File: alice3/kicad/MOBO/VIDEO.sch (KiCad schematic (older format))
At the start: 15 parts, among them P1 CONN_01X05, SW1 RESET, U1 LM2937-3.3, U2 VGA_daughter_board, U3 Propeller_P8X32A-D40, U4 24LC256, U5 Propeller_Plug, Y1 5 MHz

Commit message: Remove on/off switch.
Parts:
- C1: footprint Capacitors_ThroughHole:C_Radial_D13_L21_P5 -> Capacitors_ThroughHole:C_Radial_D8_L11.5_P3.5
- P1: footprint (none) -> Pin_Headers:Pin_Header_Angled_1x05
- Y1: footprint Crystals:Crystal_HC48-U_Vertical -> Crystals:Crystal_HC50-U_Vertical
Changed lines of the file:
@@
 $EndComp
 $Comp
-L GND #PWR10
+L GND #PWR01
 U 1 1 566E4A0D
 P 6100 4700
-F 0 "#PWR10" H 6100 4450 50  0001 C CNN
+F 0 "#PWR01" H 6100 4450 50  0001 C CNN
 F 1 "GND" H 6100 4550 50  0000 C CNN
 F 2 "" H 6100 4700 50  0000 C CNN
@@
 $EndComp
 $Comp
-L +3.3V #PWR9
+L +3.3V #PWR02
 U 1 1 566E4A37
 P 6100 2100
-F 0 "#PWR9" H 6100 1950 50  0001 C CNN
+F 0 "#PWR02" H 6100 1950 50  0001 C CNN
 F 1 "+3.3V" H 6100 2240 50  0000 C CNN
 F 2 "" H 6100 2100 50  0000 C CNN
@@
 F 0 "Y1" H 7750 4600 50  0000 C CNN
 F 1 "5 MHz" H 7750 4300 50  0000 C CNN
-F 2 "Crystals:Crystal_HC48-U_Vertical" H 7750 4450 50  0001 C CNN
+F 2 "Crystals:Crystal_HC50-U_Vertical" H 7750 4450 50  0001 C CNN
 F 3 "" H 7750 4450 50  0000 C CNN
 	1    7750 4450
@@
 $EndComp
 $Comp
-L GND #PWR14
+L GND #PWR03
 U 1 1 566E4C07
 P 8650 2400
-F 0 "#PWR14" H 8650 2150 50  0001 C CNN
+F 0 "#PWR03" H 8650 2150 50  0001 C CNN
 F 1 "GND" H 8650 2250 50  0000 C CNN
 F 2 "" H 8650 2400 50  0000 C CNN
@@
 $EndComp
 $Comp
-L GND #PWR13
+L GND #PWR04
 U 1 1 5681F164
 P 8350 4400
-F 0 "#PWR13" H 8350 4150 50  0001 C CNN
+F 0 "#PWR04" H 8350 4150 50  0001 C CNN
 F 1 "GND" H 8350 4250 50  0000 C CNN
 F 2 "" H 8350 4400 50  0000 C CNN
@@
 $EndComp
 $Comp
-L +3.3V #PWR15
+L +3.3V #PWR05
 U 1 1 5681F2C2
 P 9450 3850
-F 0 "#PWR15" H 9450 3700 50  0001 C CNN
+F 0 "#PWR05" H 9450 3700 50  0001 C CNN
 F 1 "+3.3V" H 9450 3990 50  0000 C CNN
 F 2 "" H 9450 3850 50  0000 C CNN
@@
 $EndComp
 $Comp
-L GND #PWR16
+L GND #PWR06
 U 1 1 5681F2E8
 P 9700 4150
-F 0 "#PWR16" H 9700 3900 50  0001 C CNN
+F 0 "#PWR06" H 9700 3900 50  0001 C CNN
 F 1 "GND" H 9700 4000 50  0000 C CNN
 F 2 "" H 9700 4150 50  0000 C CNN
@@
 $EndComp
 $Comp
-L +3.3V #PWR12
+L +3.3V #PWR07
 U 1 1 5681F435
 P 8100 3600
-F 0 "#PWR12" H 8100 3450 50  0001 C CNN
+F 0 "#PWR07" H 8100 3450 50  0001 C CNN
 F 1 "+3.3V" H 8100 3740 50  0000 C CNN
 F 2 "" H 8100 3600 50  0000 C CNN
@@
 $EndComp
 $Comp
-L GND #PWR2
+L GND #PWR08
 U 1 1 5681F91B
 P 2950 2350
-F 0 "#PWR2" H 2950 2100 50  0001 C CNN
+F 0 "#PWR08" H 2950 2100 50  0001 C CNN
 F 1 "GND" H 2950 2200 50  0000 C CNN
 F 2 "" H 2950 2350 50  0000 C CNN
@@
 $EndComp
 $Comp
-L +5V #PWR1
+L +5V #PWR09
 U 1 1 5681FA03
 P 2350 1650
-F 0 "#PWR1" H 2350 1500 50  0001 C CNN
+F 0 "#PWR09" H 2350 1500 50  0001 C CNN
 F 1 "+5V" H 2350 1790 50  0000 C CNN
 F 2 "" H 2350 1650 50  0000 C CNN
@@
 $EndComp
 $Comp
-L +3.3V #PWR3
+L +3.3V #PWR010
 U 1 1 5681FA32
 P 3550 1650
-F 0 "#PWR3" H 3550 1500 50  0001 C CNN
+F 0 "#PWR010" H 3550 1500 50  0001 C CNN
 F 1 "+3.3V" H 3550 1790 50  0000 C CNN
 F 2 "" H 3550 1650 50  0000 C CNN
@@
 F 0 "C1" H 3575 2100 50  0000 L CNN
 F 1 "1000 µF" H 3575 1900 50  0000 L CNN
-F 2 "Capacitors_ThroughHole:C_Radial_D13_L21_P5" H 3550 2000 50  0001 C CNN
+F 2 "Capacitors_ThroughHole:C_Radial_D8_L11.5_P3.5" H 3550 2000 50  0001 C CNN
 F 3 "" H 3550 2000 50  0000 C CNN
 	1    3550 2000
@@
 $EndComp
 $Comp
-L GND #PWR4
+L GND #PWR011
 U 1 1 56821F3F
 P 5100 2700
-F 0 "#PWR4" H 5100 2450 50  0001 C CNN
+F 0 "#PWR011" H 5100 2450 50  0001 C CNN
 F 1 "GND" H 5100 2550 50  0000 C CNN
 F 2 "" H 5100 2700 50  0000 C CNN
@@
 $EndComp
 $Comp
-L GND #PWR11
+L GND #PWR012
 U 1 1 56826035
 P 7450 2400
-F 0 "#PWR11" H 7450 2150 50  0001 C CNN
+F 0 "#PWR012" H 7450 2150 50  0001 C CNN
 F 1 "GND" H 7450 2250 50  0000 C CNN
 F 2 "" H 7450 2400 50  0000 C CNN
@@
 	8300 2500 7850 2500
 $Comp
-L GND #PWR5
+L GND #PWR013
 U 1 1 568DCD28
 P 5600 4800
-F 0 "#PWR5" H 5600 4550 50  0001 C CNN
+F 0 "#PWR013" H 5600 4550 50  0001 C CNN
 F 1 "GND" H 5600 4650 50  0000 C CNN
 F 2 "" H 5600 4800 50  0000 C CNN
@@
 	5500 4800 5600 4800
 $Comp
-L +5V #PWR8
+L +5V #PWR014
 U 1 1 568DCDF3
 P 5900 4850
-F 0 "#PWR8" H 5900 4700 50  0001 C CNN
+F 0 "#PWR014" H 5900 4700 50  0001 C CNN
 F 1 "+5V" H 5900 4990 50  0000 C CNN
 F 2 "" H 5900 4850 50  0000 C CNN
@@
 $EndComp
 $Comp
-L GND #PWR7
+L GND #PWR015
 U 1 1 568DD571
 P 5800 2200
-F 0 "#PWR7" H 5800 1950 50  0001 C CNN
+F 0 "#PWR015" H 5800 1950 50  0001 C CNN
 F 1 "GND" H 5800 2050 50  0000 C CNN
 F 2 "" H 5800 2200 50  0000 C CNN
@@
 $EndComp
 $Comp
-L +3.3V #PWR6
+L +3.3V #PWR016
 U 1 1 568DD5A9
 P 5800 1700
-F 0 "#PWR6" H 5800 1550 50  0001 C CNN
+F 0 "#PWR016" H 5800 1550 50  0001 C CNN
 F 1 "+3.3V" H 5800 1840 50  0000 C CNN
 F 2 "" H 5800 1700 50  0000 C CNN
@@
 F 0 "P1" H 3200 3900 50  0000 C CNN
 F 1 "CONN_01X05" V 3300 3600 50  0000 C CNN
-F 2 "" H 3200 3600 50  0000 C CNN
+F 2 "Pin_Headers:Pin_Header_Angled_1x05" H 3200 3600 50  0001 C CNN
 F 3 "" H 3200 3600 50  0000 C CNN
 	1    3200 3600
@@
 $EndComp
 $Comp
-L GND #PWR?
+L GND #PWR017
 U 1 1 56A0506B
 P 3400 3900
-F 0 "#PWR?" H 3400 3650 50  0001 C CNN
+F 0 "#PWR017" H 3400 3650 50  0001 C CNN
 F 1 "GND" H 3400 3750 50  0000 C CNN
 F 2 "" H 3400 3900 50  0000 C CNN
@@
 $EndComp
 $Comp
-L +3.3V #PWR?
+L +3.3V #PWR018
 U 1 1 56A050A3
 P 3700 3900
-F 0 "#PWR?" H 3700 3750 50  0001 C CNN
+F 0 "#PWR018" H 3700 3750 50  0001 C CNN
 F 1 "+3.3V" H 3700 4040 50  0000 C CNN
 F 2 "" H 3700 3900 50  0000 C CNN

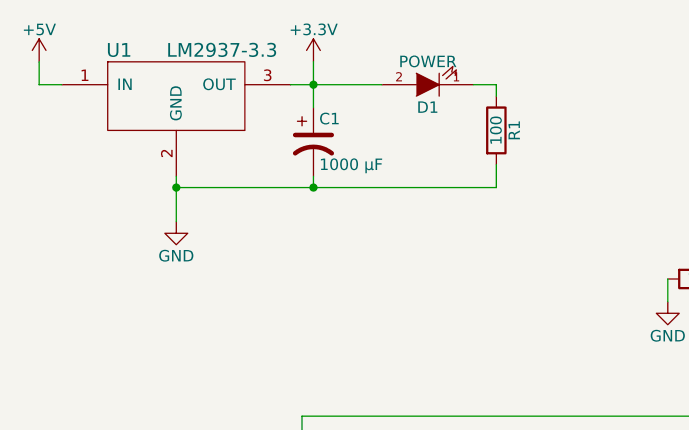
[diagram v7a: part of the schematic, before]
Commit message: Remove DFROBOT and LDO.
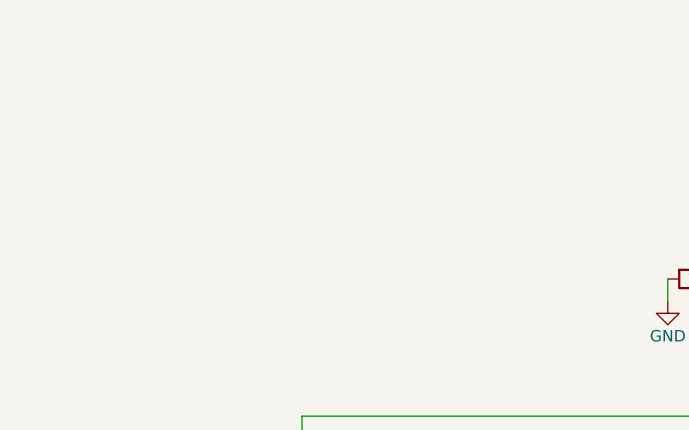
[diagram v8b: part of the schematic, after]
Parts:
- removed C1: 1000 µF, Capacitors_ThroughHole:C_Radial_D8_L11.5_P3.5, symbol CP1
- removed D1: POWER, LEDs:LED-5MM, symbol LED
- removed R1: 100, Resistors_ThroughHole:Resistor_Horizontal_RM10mm, symbol R
- removed U1: LM2937-3.3, Power_Integrations:TO-220, symbol LM2937-3.3
- U5: footprint Pin_Headers:Pin_Header_Straight_1x04 -> Pin_Headers:Pin_Header_Angled_1x04
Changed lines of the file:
@@
 $EndComp
 $Comp
-L GND #PWR12
+L GND #PWR01
 U 1 1 566E4A0D
 P 6100 4700
-F 0 "#PWR12" H 6100 4450 50  0001 C CNN
+F 0 "#PWR01" H 6100 4450 50  0001 C CNN
 F 1 "GND" H 6100 4550 50  0000 C CNN
 F 2 "" H 6100 4700 50  0000 C CNN
@@
 $EndComp
 $Comp
-L +3.3V #PWR11
+L +3.3V #PWR02
 U 1 1 566E4A37
 P 6100 2100
-F 0 "#PWR11" H 6100 1950 50  0001 C CNN
+F 0 "#PWR02" H 6100 1950 50  0001 C CNN
 F 1 "+3.3V" H 6100 2240 50  0000 C CNN
 F 2 "" H 6100 2100 50  0000 C CNN
@@
 $EndComp
 $Comp
-L GND #PWR16
+L GND #PWR03
 U 1 1 566E4C07
 P 8650 2400
-F 0 "#PWR16" H 8650 2150 50  0001 C CNN
+F 0 "#PWR03" H 8650 2150 50  0001 C CNN
 F 1 "GND" H 8650 2250 50  0000 C CNN
 F 2 "" H 8650 2400 50  0000 C CNN
@@
 $EndComp
 $Comp
-L GND #PWR15
+L GND #PWR04
 U 1 1 5681F164
 P 8350 4400
-F 0 "#PWR15" H 8350 4150 50  0001 C CNN
+F 0 "#PWR04" H 8350 4150 50  0001 C CNN
 F 1 "GND" H 8350 4250 50  0000 C CNN
 F 2 "" H 8350 4400 50  0000 C CNN
@@
 $EndComp
 $Comp
-L +3.3V #PWR17
+L +3.3V #PWR05
 U 1 1 5681F2C2
 P 9450 3850
-F 0 "#PWR17" H 9450 3700 50  0001 C CNN
+F 0 "#PWR05" H 9450 3700 50  0001 C CNN
 F 1 "+3.3V" H 9450 3990 50  0000 C CNN
 F 2 "" H 9450 3850 50  0000 C CNN
@@
 $EndComp
 $Comp
-L GND #PWR18
+L GND #PWR06
 U 1 1 5681F2E8
 P 9700 4150
-F 0 "#PWR18" H 9700 3900 50  0001 C CNN
+F 0 "#PWR06" H 9700 3900 50  0001 C CNN
 F 1 "GND" H 9700 4000 50  0000 C CNN
 F 2 "" H 9700 4150 50  0000 C CNN
@@
 $EndComp
 $Comp
-L +3.3V #PWR14
+L +3.3V #PWR07
 U 1 1 5681F435
 P 8100 3600
-F 0 "#PWR14" H 8100 3450 50  0001 C CNN
+F 0 "#PWR07" H 8100 3450 50  0001 C CNN
 F 1 "+3.3V" H 8100 3740 50  0000 C CNN
 F 2 "" H 8100 3600 50  0000 C CNN
@@
 F 0 "U5" H 9500 3150 60  0000 C CNN
 F 1 "Propeller_Plug" H 9650 2500 60  0000 C CNN
-F 2 "Pin_Headers:Pin_Header_Straight_1x04" H 9600 2850 60  0001 C CNN
+F 2 "Pin_Headers:Pin_Header_Angled_1x04" H 9600 2850 60  0001 C CNN
 F 3 "" H 9600 2850 60  0000 C CNN
 	1    9600 2850
-	1    0    0    -1
-$EndComp
-$Comp
-L LM2937-3.3 U1
-U 1 1 5681F8BE
-P 2950 1800
-F 0 "U1" H 2700 2000 60  0000 C CNN
-F 1 "LM2937-3.3" H 3150 2000 60  0000 C CNN
-F 2 "Power_Integrations:TO-220" H 2950 1800 60  0001 C CNN
-F 3 "" H 2950 1800 60  0000 C CNN
-	1    2950 1800
-	1    0    0    -1
-$EndComp
-$Comp
-L GND #PWR2
-U 1 1 5681F91B
-P 2950 2350
-F 0 "#PWR2" H 2950 2100 50  0001 C CNN
-F 1 "GND" H 2950 2200 50  0000 C CNN
-F 2 "" H 2950 2350 50  0000 C CNN
-F 3 "" H 2950 2350 50  0000 C CNN
-	1    2950 2350
-	1    0    0    -1
-$EndComp
-$Comp
-L +5V #PWR1
-U 1 1 5681FA03
-P 2350 1650
-F 0 "#PWR1" H 2350 1500 50  0001 C CNN
-F 1 "+5V" H 2350 1790 50  0000 C CNN
-F 2 "" H 2350 1650 50  0000 C CNN
-F 3 "" H 2350 1650 50  0000 C CNN
-	1    2350 1650
-	1    0    0    -1
-$EndComp
-$Comp
-L +3.3V #PWR4
-U 1 1 5681FA32
-P 3550 1650
-F 0 "#PWR4" H 3550 1500 50  0001 C CNN
-F 1 "+3.3V" H 3550 1790 50  0000 C CNN
-F 2 "" H 3550 1650 50  0000 C CNN
-F 3 "" H 3550 1650 50  0000 C CNN
-	1    3550 1650
-	1    0    0    -1
-$EndComp
-$Comp
-L CP1 C1
-U 1 1 5681FB9D
-P 3550 2000
-F 0 "C1" H 3575 2100 50  0000 L CNN
-F 1 "1000 µF" H 3575 1900 50  0000 L CNN
-F 2 "Capacitors_ThroughHole:C_Radial_D8_L11.5_P3.5" H 3550 2000 50  0001 C CNN
-F 3 "" H 3550 2000 50  0000 C CNN
-	1    3550 2000
-	1    0    0    -1
-$EndComp
-$Comp
-L LED D1
-U 1 1 5681FD4E
-P 4050 1750
-F 0 "D1" H 4050 1850 50  0000 C CNN
-F 1 "POWER" H 4050 1650 50  0000 C CNN
-F 2 "LEDs:LED-5MM" H 4050 1750 50  0001 C CNN
-F 3 "" H 4050 1750 50  0000 C CNN
-	1    4050 1750
-	-1   0    0    1
-$EndComp
-$Comp
-L R R1
-U 1 1 5681FD9C
-P 4350 1950
-F 0 "R1" V 4430 1950 50  0000 C CNN
-F 1 "100" V 4350 1950 50  0000 C CNN
-F 2 "Resistors_ThroughHole:Resistor_Horizontal_RM10mm" V 4280 1950 50  0001 C CNN
-F 3 "" H 4350 1950 50  0000 C CNN
-	1    4350 1950
 	1    0    0    -1
 $EndComp
@@
 $EndComp
 $Comp
-L GND #PWR6
+L GND #PWR08
 U 1 1 56821F3F
 P 5100 2700
-F 0 "#PWR6" H 5100 2450 50  0001 C CNN
+F 0 "#PWR08" H 5100 2450 50  0001 C CNN
 F 1 "GND" H 5100 2550 50  0000 C CNN
 F 2 "" H 5100 2700 50  0000 C CNN
@@
 $EndComp
 $Comp
-L GND #PWR13
+L GND #PWR09
 U 1 1 56826035
 P 7450 2400
-F 0 "#PWR13" H 7450 2150 50  0001 C CNN
+F 0 "#PWR09" H 7450 2150 50  0001 C CNN
 F 1 "GND" H 7450 2250 50  0000 C CNN
 F 2 "" H 7450 2400 50  0000 C CNN
@@
 Connection ~ 8650 2300
 Wire Wire Line
-	2950 2150 2950 2350
-Wire Wire Line
-	2450 1750 2350 1750
-Wire Wire Line
-	2350 1750 2350 1650
-Wire Wire Line
-	3450 1750 3850 1750
-Wire Wire Line
-	3550 1650 3550 1850
-Connection ~ 3550 1750
-Wire Wire Line
-	3550 2150 3550 2200
-Wire Wire Line
-	2950 2200 4350 2200
-Connection ~ 2950 2200
-Wire Wire Line
-	4250 1750 4350 1750
-Wire Wire Line
-	4350 1750 4350 1800
-Wire Wire Line
-	4350 2200 4350 2100
-Connection ~ 3550 2200
-Wire Wire Line
 	5900 2600 6200 2600
 Wire Wire Line
@@
 	8300 2500 7850 2500
 $Comp
-L GND #PWR7
+L GND #PWR010
 U 1 1 568DCD28
 P 5600 4800
-F 0 "#PWR7" H 5600 4550 50  0001 C CNN
+F 0 "#PWR010" H 5600 4550 50  0001 C CNN
 F 1 "GND" H 5600 4650 50  0000 C CNN
 F 2 "" H 5600 4800 50  0000 C CNN
@@
 	5500 4800 5600 4800
 $Comp
-L +5V #PWR10
+L +5V #PWR011
 U 1 1 568DCDF3
 P 5900 4850
-F 0 "#PWR10" H 5900 4700 50  0001 C CNN
+F 0 "#PWR011" H 5900 4700 50  0001 C CNN
 F 1 "+5V" H 5900 4990 50  0000 C CNN
 F 2 "" H 5900 4850 50  0000 C CNN
@@
 $EndComp
 $Comp
-L GND #PWR9
+L GND #PWR012
 U 1 1 568DD571
 P 5800 2200
-F 0 "#PWR9" H 5800 1950 50  0001 C CNN
+F 0 "#PWR012" H 5800 1950 50  0001 C CNN
 F 1 "GND" H 5800 2050 50  0000 C CNN
 F 2 "" H 5800 2200 50  0000 C CNN
@@
 $EndComp
 $Comp
-L +3.3V #PWR8
+L +3.3V #PWR013
 U 1 1 568DD5A9
 P 5800 1700
-F 0 "#PWR8" H 5800 1550 50  0001 C CNN
+F 0 "#PWR013" H 5800 1550 50  0001 C CNN
 F 1 "+3.3V" H 5800 1840 50  0000 C CNN
 F 2 "" H 5800 1700 50  0000 C CNN
@@
 $EndComp
 $Comp
-L GND #PWR3
+L GND #PWR014
 U 1 1 56A0506B
 P 3400 3900
-F 0 "#PWR3" H 3400 3650 50  0001 C CNN
+F 0 "#PWR014" H 3400 3650 50  0001 C CNN
 F 1 "GND" H 3400 3750 50  0000 C CNN
 F 2 "" H 3400 3900 50  0000 C CNN
@@
 $EndComp
 $Comp
-L +3.3V #PWR5
+L +3.3V #PWR015
 U 1 1 56A050A3
 P 3700 3900
-F 0 "#PWR5" H 3700 3750 50  0001 C CNN
+F 0 "#PWR015" H 3700 3750 50  0001 C CNN
 F 1 "+3.3V" H 3700 4040 50  0000 C CNN
 F 2 "" H 3700 3900 50  0000 C CNN
